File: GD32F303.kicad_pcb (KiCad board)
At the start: 4 copper layers, 100 x 60 mm, 127 parts, among them CN1 KF128L-5.08-2P, CN2 WJ15EDGRC-3.81-2P, CN4 WJ15EDGRC-3.81-2P, J1 TYPE-C-31-M-31, J2 TYPE-C 16PIN 2MD(073), Q1 CJ3134K KF, Q2 CJ3134K KF, SW1 SKRPACE010, U1 XL1509-5.0, U10 SIT3485ESA, U11 TXS0104EPWR, U12 TXS0104EPWR, U13 CH340E, U14 TPD4S012DRYR, U2 B0503S-2WR3L, U3 SY8089A1AAC, U4 CH213K, U5 SY8089AAC, U6 GD32F303VCT6, U7 ISO1050DWR, U9 π131U30, Y1 TAXM8M4RDBCCT2T, Y2 XKXGI-SUA-32.768K

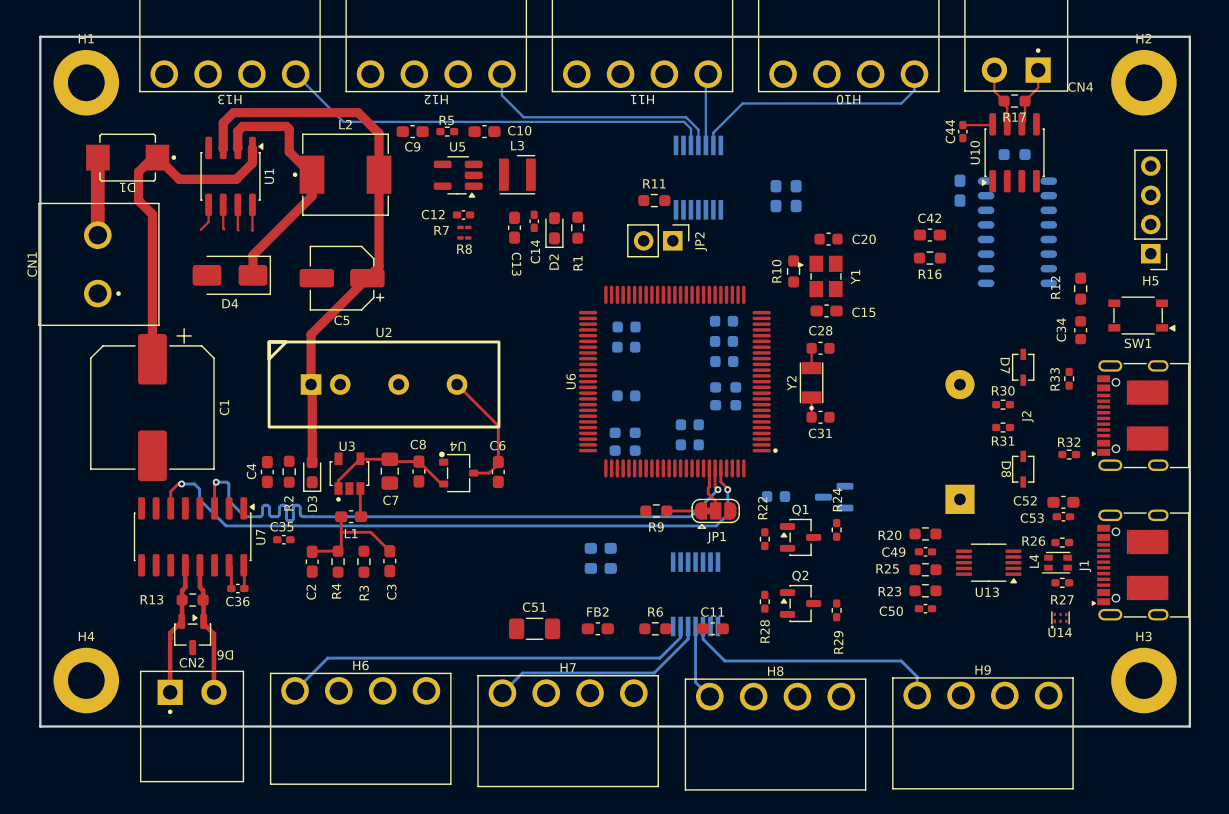
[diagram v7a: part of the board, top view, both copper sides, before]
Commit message: 完善总线映射并划分隔离地与电源平面
统一3V3电源网络并消除ERC错误；优化GND/Earth耦合器件布局；完成In1.Cu地平面及In2.Cu电源平面分区。
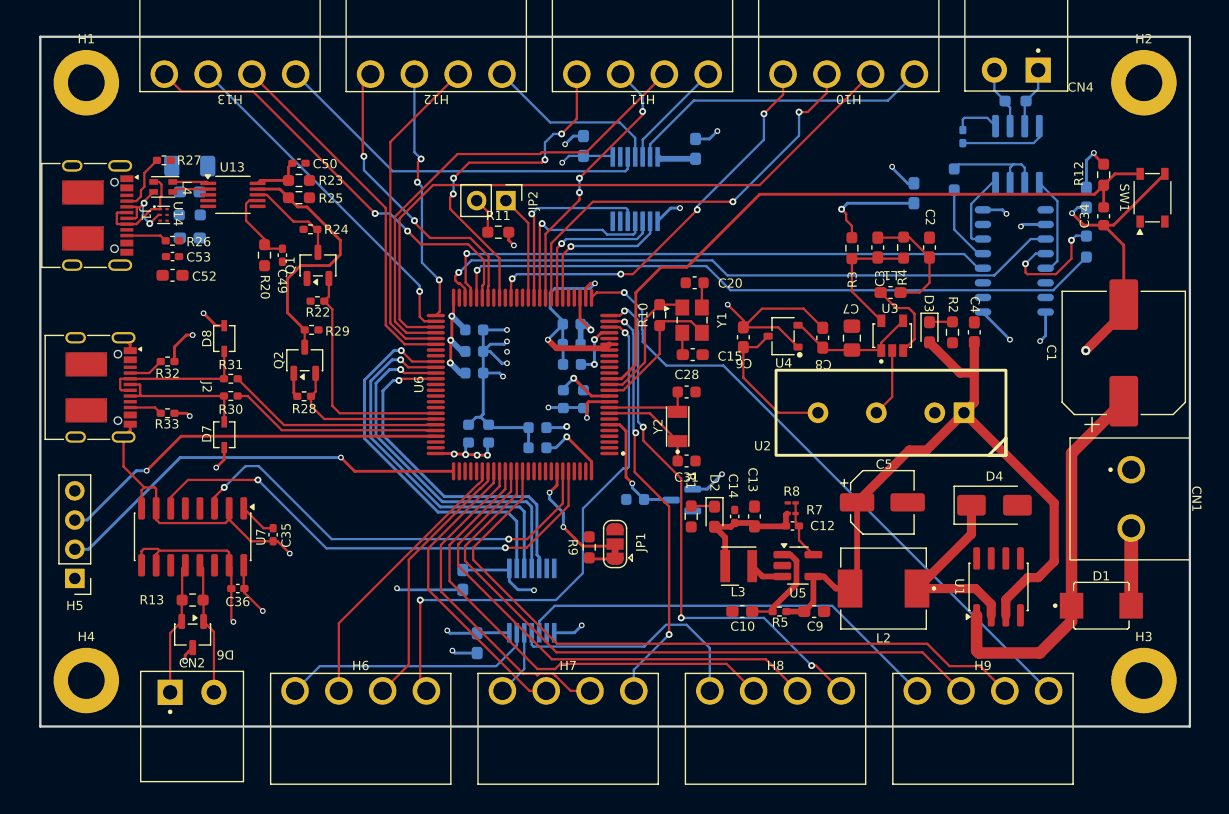
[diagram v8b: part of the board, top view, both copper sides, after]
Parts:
- removed B01: VBAT_BAT, Battery:BatteryHolder_Keystone_500
- C11, C42, C44, C51, FB2, R16, R17, R6, U10: moved to B.Cu
- moved H5 97.8 mm to (88.5, 106.1)
- moved D1 93.2 mm to (177.8, 108.5), turned to 0 degrees
- moved J1 92.3 mm to (92.0, 74.5), turned to -90 degrees
- moved CN1 92.2 mm to (180.4, 99.2), turned to -90 degrees
- moved J2 86.9 mm to (92.2, 89.5), turned to -90 degrees
- moved R27 86.4 mm to (96.2, 69.8), turned to 180 degrees
- moved U14 85.5 mm to (96.2, 74.5), turned to 0 degrees
- moved C1 84.6 mm to (179.8, 86.5), turned to 90 degrees
- moved L4 84.4 mm to (96.2, 72.1), turned to -90 degrees
- moved R26 81.7 mm to (97.0, 76.8), turned to 180 degrees
- moved C53 80.7 mm to (97.0, 78.1), turned to 0 degrees
- moved C52 80.0 mm to (97.0, 79.8), turned to 0 degrees
- moved R32 78.8 mm to (96.6, 87.2), turned to 180 degrees
- moved R33 78.5 mm to (96.6, 91.8), turned to 0 degrees
- moved U1 75.8 mm to (168.9, 106.9), turned to 90 degrees
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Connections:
- net /MCU_Core/USB_DM renamed /MCU_Core/USB_DN
- C16 pad 1: +3.3V -> +3V3
- C17 pad 1: +3.3V -> +3V3
- C18 pad 1: +3.3V -> +3V3
- C19 pad 1: +3.3V -> +3V3
- C22 pad 1: +3.3V -> +3V3
- C23 pad 1: +3.3V -> +3V3
- C24 pad 1: +3.3V -> +3V3
- C25 pad 1: +3.3V -> +3V3
- C26 pad 1: +3.3V -> +3V3
- C27 pad 1: +3.3V -> +3V3
- C29 pad 1: +3.3V -> +3V3
- C30 pad 1: +3.3V -> +3V3
- C35 pad 1: +3.3V_ISO -> +3V3
- C42 pad 2: +3.3V -> +3V3
- C45 pad 1: +3.3V -> +3V3
- C46 pad 1: +3.3V -> +3V3
- CN4 pad 1: /RS485/RS485A -> /RS485/RS485B
- CN4 pad 2: /RS485/RS485B -> /RS485/RS485A
- D5 pad 1: +3.3V -> +3V3
- H5 pad 4: +3.3V -> +3V3
- JP1 pad 3: +3.3V -> +3V3
- R12 pad 2: +3.3V -> +3V3
- U11 pad 1: +3.3V -> +3V3
- U11 pad 8: +3.3V -> +3V3
- U12 pad 1: +3.3V -> +3V3
- U12 pad 8: +3.3V -> +3V3
- U6 pad 100: +3.3V -> +3V3
- U6 pad 11: +3.3V -> +3V3
- U6 pad 21: +3.3V -> +3V3
- U6 pad 22: +3.3V -> +3V3
- U6 pad 28: +3.3V -> +3V3
- U6 pad 50: +3.3V -> +3V3
- U6 pad 51: unconnected-(U6E-PB12-Pad51) -> /MCU_Core/DIR2_3
- U6 pad 52: unconnected-(U6E-PB13-Pad52) -> /MCU_Core/DIR2_4
- U6 pad 53: unconnected-(U6E-PB14-Pad53) -> /MCU_Core/BRAKE2_1
- U6 pad 54: unconnected-(U6E-PB15-Pad54) -> /MCU_Core/BRAKE2_2
- U6 pad 55: unconnected-(U6E-PD8-Pad55) -> /MCU_Core/BRAKE2_3
- U6 pad 56: unconnected-(U6E-PD9-Pad56) -> /MCU_Core/BRAKE2_4
- U6 pad 63: /MCU_Core/DIR2_3 -> unconnected-(U6C-DIR3-Pad63)
- U6 pad 64: /MCU_Core/DIR2_4 -> unconnected-(U6C-DIR4-Pad64)
- U6 pad 75: +3.3V -> +3V3
- U6 pad 81: /MCU_Core/DIR1_1 -> /MCU_Core/BRAKE1_1
- U6 pad 82: /MCU_Core/DIR1_2 -> /MCU_Core/DIR1_1
- U6 pad 83: /MCU_Core/DIR1_3 -> /MCU_Core/BRAKE1_2
- U6 pad 84: /MCU_Core/DIR1_4 -> /MCU_Core/DIR1_2
- U6 pad 85: /MCU_Core/BRAKE1_1 -> /MCU_Core/BRAKE1_3
- U6 pad 86: /MCU_Core/BRAKE1_2 -> /MCU_Core/DIR1_3
- U6 pad 87: /MCU_Core/BRAKE1_3 -> /MCU_Core/BRAKE1_4
- U6 pad 88: /MCU_Core/BRAKE1_4 -> /MCU_Core/DIR1_4
- U6 pad 89: /MCU_Core/BRAKE2_1 -> unconnected-(U6E-PB3-Pad89)
- U6 pad 90: /MCU_Core/BRAKE2_2 -> unconnected-(U6E-PB4-Pad90)
- U6 pad 91: /MCU_Core/BRAKE2_3 -> unconnected-(U6E-PB5-Pad91)
- U6 pad 92: /MCU_Core/BRAKE2_4 -> unconnected-(U6E-PB6-Pad92)
- U7 pad 1: +3.3V_ISO -> +3V3
- U9 pad 1: +3.3V -> +3V3
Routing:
- net Earth: track 0.00 -> 262.8 mm
- net GND: track 9.12 -> 132.6 mm, vias 0 -> 23
- net +3V3: track 0.00 -> 85.3 mm, vias 0 -> 19
- net /MCU_Core/DIR1_4: track 0.00 -> 60.5 mm
- net /MCU_Core/NRST: track 0.00 -> 59.1 mm
- net /MCU_Core/BRAKE2_1: track 0.00 -> 58.4 mm
- net /MCU_Core/RS485_DE: track 0.00 -> 57.6 mm, vias 0 -> 1
- net /MCU_Core/BRAKE1_4: track 0.00 -> 57.5 mm
- net /MCU_Core/RS485_RX: track 0.00 -> 56.1 mm, vias 0 -> 1
- net /MCU_Core/FG1_4: track 0.00 -> 55.9 mm, vias 0 -> 1
- net GNDS: track 2.10 -> 57.2 mm, vias 0 -> 5
- net /MCU_Core/RS485_TX: track 0.00 -> 49.5 mm, vias 0 -> 1
- net /MCU_Core/FG1_1: track 0.00 -> 48.5 mm, vias 0 -> 2
- net /MCU_Core/FG1_3: track 0.00 -> 47.3 mm, vias 0 -> 4
- net /MCU_Core/DIR1_3: track 0.00 -> 44.1 mm
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- added copper zone on In2.Cu, net +3V3
- added copper zone on In2.Cu, net +3V3_ISO
- added copper zone on In2.Cu, net +5V
- added copper zone on In2.Cu, net +5V_ISO
- added copper zone on In1.Cu, net Earth
- added copper zone on In1.Cu, net GND
- added copper zone on In1.Cu, net GNDS
